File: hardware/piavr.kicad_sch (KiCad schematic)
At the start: 6 parts, among them J1 GPIO, U1 CAT24C256

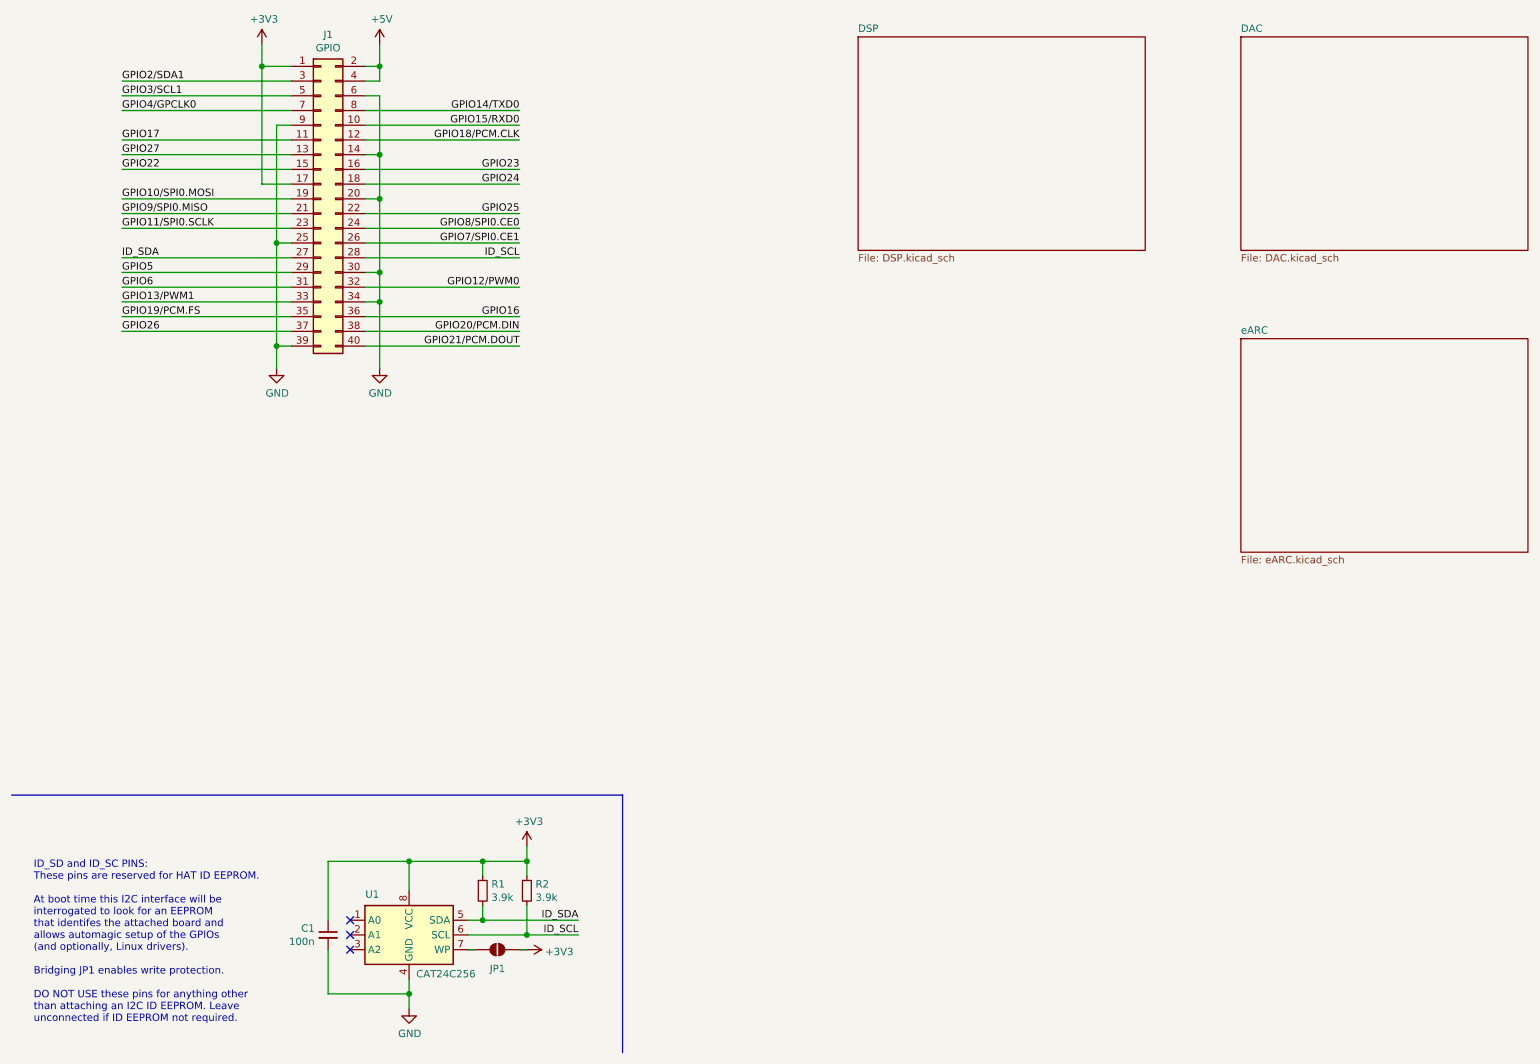
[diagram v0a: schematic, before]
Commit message: finished eARC and started with DSP
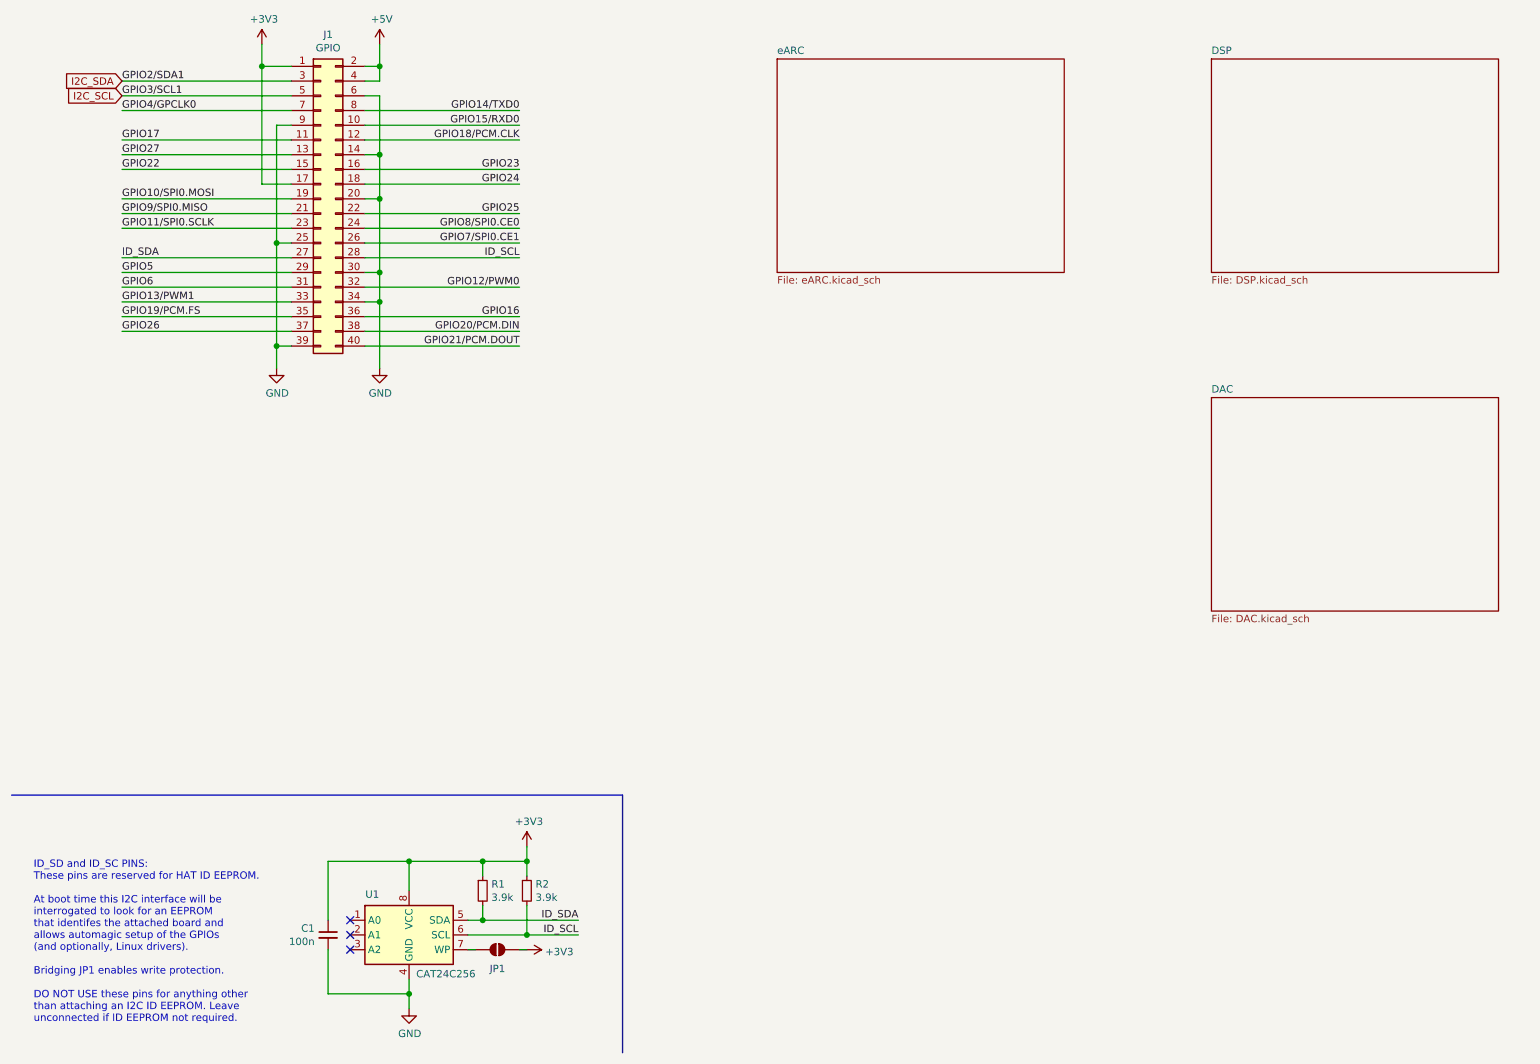
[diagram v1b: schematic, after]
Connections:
- net GPIO2/SDA1 renamed I2C_SDA
- net GPIO3/SCL1 renamed I2C_SCL
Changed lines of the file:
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@@
+		)
+	)
+	(global_label "I2C_SCL"
+		(shape input)
+		(at 31.75 33.02 180)
+		(fields_autoplaced yes)
+		(effects
+			(font
+				(size 1.27 1.27)
+			)
+			(justify right)
+		)
+		(property "Intersheetrefs" "${INTERSHEET_REFS}"
+			(at 21.1102 33.02 0)
+			(hide yes)
+			(show_name no)
+			(do_not_autoplace no)
+			(effects
+				(font
+					(size 1.27 1.27)
+				)
+				(justify right)
+			)
+		)
+	)
+	(global_label "I2C_SDA"
+		(shape input)
+		(at 31.75 30.48 180)
+		(fields_autoplaced yes)
+		(effects
+			(font
+				(size 1.27 1.27)
+			)
+			(justify right)
+		)
+		(property "Intersheetrefs" "${INTERSHEET_REFS}"
+			(at 21.0497 30.48 0)
+			(hide yes)
+			(show_name no)
+			(do_not_autoplace no)
+			(effects
+				(font
+					(size 1.27 1.27)
+				)
+				(justify right)
+			)
 		)
 	)
@@
 		(in_pos_files yes)
 		(dnp no)
-		(property "Reference" "#PWR01"
+		(property "Reference" "#PWR03"
 			(at 76.2 27.94 0)
 			(hide yes)
@@
 			(project "piavr"
 				(path "/e63e39d7-6ac0-4ffd-8aa3-1841a4541b55"
-					(reference "#PWR01")
+					(reference "#PWR03")
 					(unit 1)
 				)
@@
 		(in_pos_files yes)
 		(dnp no)
-		(property "Reference" "#PWR04"
+		(property "Reference" "#PWR01"
 			(at 55.88 27.94 0)
 			(hide yes)
@@
 			(project "piavr"
 				(path "/e63e39d7-6ac0-4ffd-8aa3-1841a4541b55"
-					(reference "#PWR04")
+					(reference "#PWR01")
 					(unit 1)
 				)
@@
 		(in_pos_files yes)
 		(dnp no)
-		(property "Reference" "#PWR02"
+		(property "Reference" "#PWR04"
 			(at 76.2 86.36 0)
 			(hide yes)
@@
 			(project "piavr"
 				(path "/e63e39d7-6ac0-4ffd-8aa3-1841a4541b55"
-					(reference "#PWR02")
+					(reference "#PWR04")
 					(unit 1)
 				)
@@
 		(in_pos_files yes)
 		(dnp no)
-		(property "Reference" "#PWR03"
+		(property "Reference" "#PWR02"
 			(at 58.42 86.36 0)
 			(hide yes)
@@
 			(project "piavr"
 				(path "/e63e39d7-6ac0-4ffd-8aa3-1841a4541b55"
-					(reference "#PWR03")
+					(reference "#PWR02")
 					(unit 1)
 				)
@@
 		(in_pos_files yes)
 		(dnp no)
-		(property "Reference" "#PWR0101"
+		(property "Reference" "#PWR06"
 			(at 101.6 166.37 0)
 			(hide yes)
@@
 			(project "piavr"
 				(path "/e63e39d7-6ac0-4ffd-8aa3-1841a4541b55"
-					(reference "#PWR0101")
+					(reference "#PWR06")
 					(unit 1)
 				)
@@
 		(in_pos_files yes)
 		(dnp no)
-		(property "Reference" "#PWR0102"
+		(property "Reference" "#PWR05"
 			(at 81.28 196.85 0)
 			(hide yes)
@@
 			(project "piavr"
 				(path "/e63e39d7-6ac0-4ffd-8aa3-1841a4541b55"
-					(reference "#PWR0102")
+					(reference "#PWR05")
 					(unit 1)
 				)
@@
 		(in_pos_files yes)
 		(dnp no)
-		(property "Reference" "#PWR0103"
+		(property "Reference" "#PWR07"
 			(at 97.79 180.34 0)
 			(hide yes)
@@
 			(project "piavr"
 				(path "/e63e39d7-6ac0-4ffd-8aa3-1841a4541b55"
-					(reference "#PWR0103")
+					(reference "#PWR07")
 					(unit 1)
 				)
@@
 	)
 	(sheet
-		(at 224.79 22.86)
+		(at 219.71 85.09)
 		(size 49.53 36.83)
 		(exclude_from_sim no)
@@
 		)
 		(property "Sheetname" "DAC"
-			(at 224.79 22.1484 0)
+			(at 219.71 84.3784 0)
 			(show_name no)
 			(do_not_autoplace no)
@@
 		)
 		(property "Sheetfile" "DAC.kicad_sch"
-			(at 224.79 60.2746 0)
+			(at 219.71 122.5046 0)
 			(show_name no)
 			(do_not_autoplace no)
@@
 	)
 	(sheet
-		(at 224.79 74.93)
+		(at 144.78 26.67)
 		(size 49.53 36.83)
 		(exclude_from_sim no)
@@
 		)
 		(property "Sheetname" "eARC"
-			(at 224.79 74.2184 0)
+			(at 144.78 25.9584 0)
 			(show_name no)
 			(do_not_autoplace no)
@@
 		)
 		(property "Sheetfile" "eARC.kicad_sch"
-			(at 224.79 112.3446 0)
+			(at 144.78 64.0846 0)
 			(show_name no)
 			(do_not_autoplace no)
@@
 	)
 	(sheet
-		(at 158.75 22.86)
+		(at 219.71 26.67)
 		(size 49.53 36.83)
 		(exclude_from_sim no)
@@
 		)
 		(property "Sheetname" "DSP"
-			(at 158.75 22.1484 0)
+			(at 219.71 25.9584 0)
 			(show_name no)
 			(do_not_autoplace no)
@@
 		)
 		(property "Sheetfile" "DSP.kicad_sch"
-			(at 158.75 60.2746 0)
-			(show_name no)
-			(do_not_autoplace no)
+			(at 219.71 64.0846 0)
+			(show_name no)
+			(do_not_autoplace no)
